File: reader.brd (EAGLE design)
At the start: 41.6 x 39.4 mm, 15 parts, among them J1 RJ11-6PTH, J2 AVR_SPI_PRG_6NS

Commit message: Change sound source select jumpers to a single 3-pin jumper
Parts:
- removed JP3: (no value), SparkFun-Retired:1X02
- JP2: device SparkFun-Retired:1X02 -> jumper:JP2
- moved JP2 1.27 mm to (20.3, 25.4), turned to 90 degrees
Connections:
- removed net N$4: JP2.2, JP3.2, SP1.1
- new net N$1: JP2.2, SP1.1
- net N$9: now also JP2.3; no longer JP3.1
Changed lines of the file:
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@@
 <element name="J2" library="SparkFun-Connectors" package="2X3-NS" value="AVR_SPI_PRG_6NS" x="35.56" y="34.29"/>
 <element name="JP1" library="SparkFun-Connectors" package="1X08" value="MFRC522 Module" x="25.4" y="10.16" rot="R90"/>
-<element name="JP2" library="SparkFun-Retired" package="1X02" value="" x="19.05" y="25.4" rot="R270"/>
-<element name="JP3" library="SparkFun-Retired" package="1X02" value="" x="21.59" y="25.4" rot="R270"/>
 <element name="LD1" library="led" package="DUOLED-C-5MM" value="STATUS" x="1.27" y="34.29" rot="R90"/>
 <element name="LED1" library="led" package="LED3MM" value="BLUE" x="1.27" y="2.54" rot="R90"/>
@@
 <attribute name="OC_FARNELL" value="unknown" x="11.43" y="11.43" size="1.778" layer="27" rot="R180" display="off"/>
 </element>
+<element name="JP2" library="jumper" package="JP2" value="" x="20.32" y="25.4" rot="R90"/>
 </elements>
 <signals>
@@
 </signal>
 <signal name="EXT_SPEAKER">
+<contactref element="J1" pad="6"/>
 <contactref element="JP2" pad="1"/>
-<contactref element="J1" pad="6"/>
-<wire x1="6.985" y1="27.94" x2="19.05" y2="25.4" width="0" layer="19" extent="1-1"/>
+<wire x1="20.32" y1="22.86" x2="6.985" y2="27.94" width="0" layer="19" extent="1-1"/>
 </signal>
 <signal name="SPEAKER">
@@
 </signal>
 <signal name="N$9">
-<contactref element="JP3" pad="1"/>
 <contactref element="R4" pad="2"/>
-<wire x1="21.59" y1="25.4" x2="38.1" y2="27.57" width="0" layer="19" extent="16-16"/>
+<contactref element="JP2" pad="3"/>
+<wire x1="20.32" y1="27.94" x2="38.1" y2="27.57" width="0" layer="19" extent="16-16"/>
 </signal>
-<signal name="N$4">
+<signal name="N$1">
+<contactref element="SP1" pad="1"/>
 <contactref element="JP2" pad="2"/>
-<contactref element="JP3" pad="2"/>
-<contactref element="SP1" pad="1"/>
-<wire x1="19.05" y1="22.86" x2="21.59" y2="22.86" width="0" layer="19" extent="1-1"/>
-<wire x1="16.4338" y1="11.43" x2="19.05" y2="22.86" width="0" layer="19" extent="1-1"/>
+<wire x1="20.32" y1="25.4" x2="16.4338" y2="11.43" width="0" layer="19" extent="1-1"/>
 </signal>
 </signals>

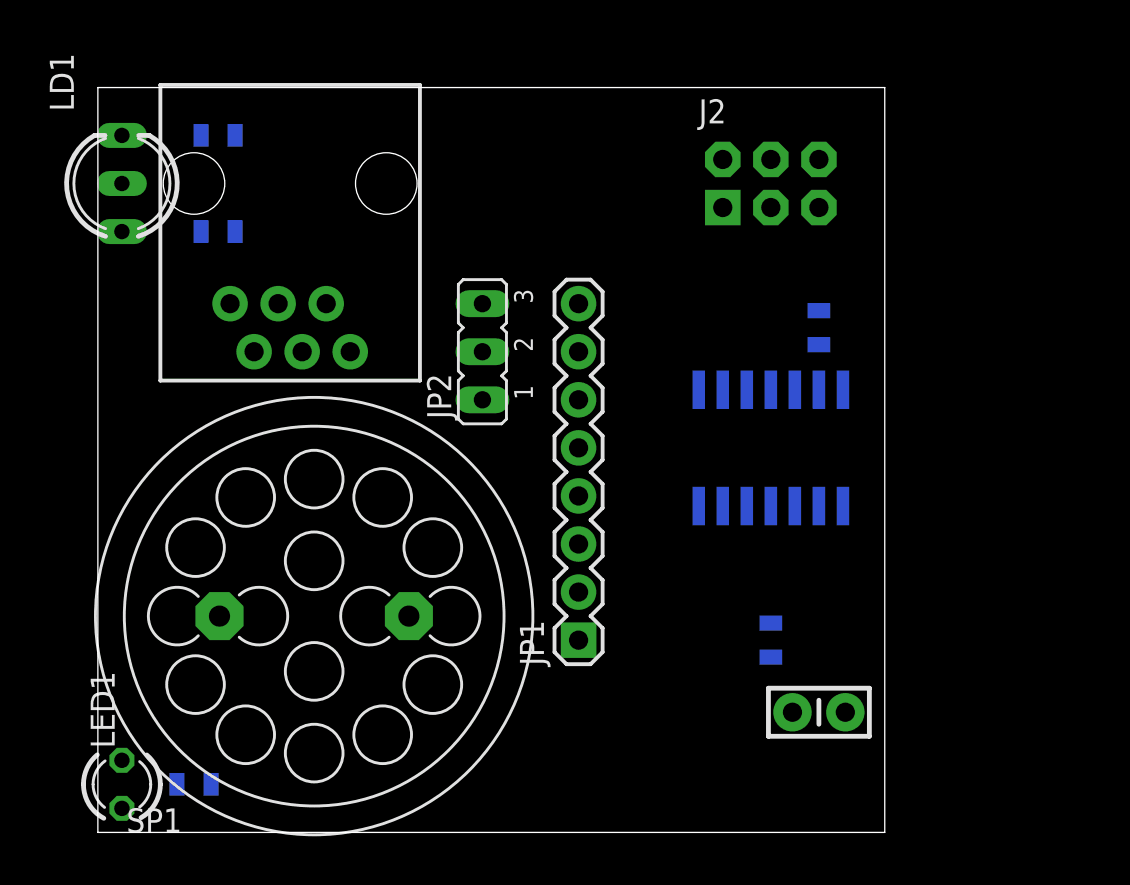
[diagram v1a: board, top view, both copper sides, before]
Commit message: Route reader board prototype
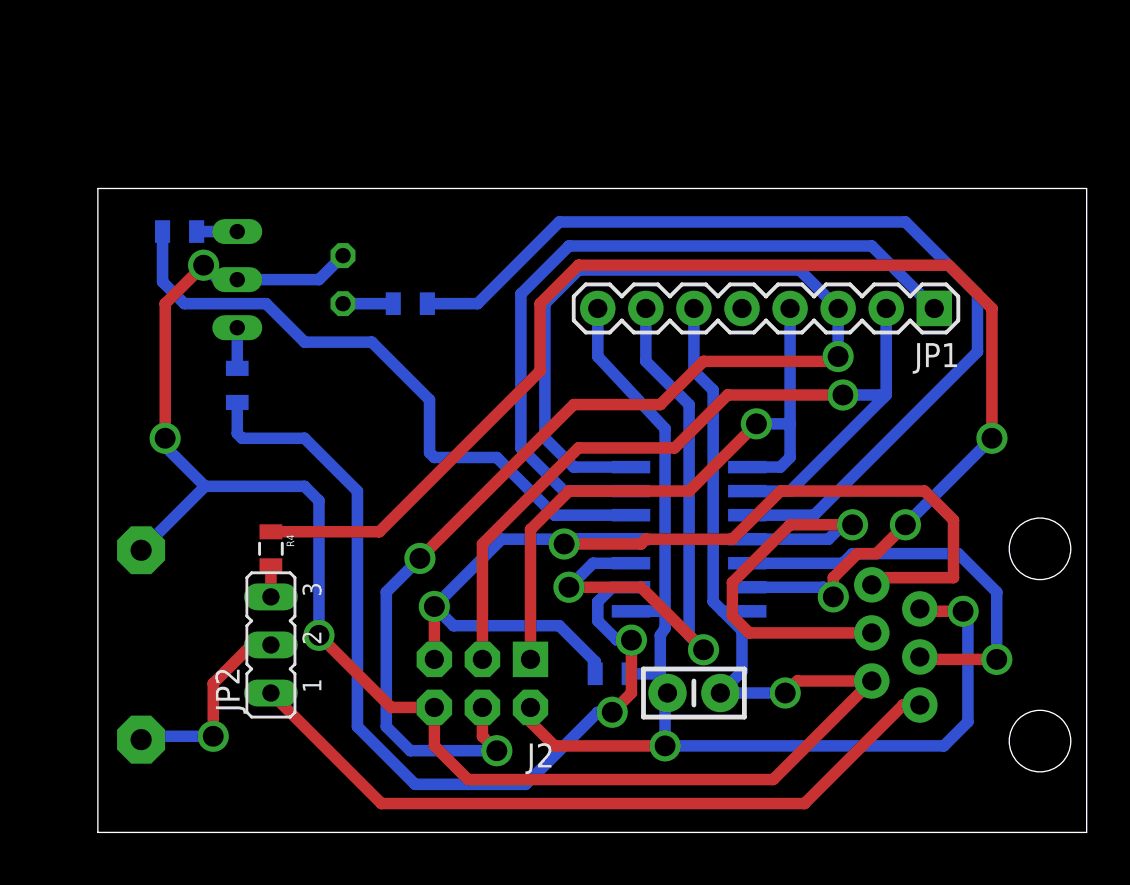
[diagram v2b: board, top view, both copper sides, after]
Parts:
- moved J1 39.6 mm to (49.8, 15.0), flipped to the bottom, turned to 270 degrees
- moved R4 31.2 mm to (9.14, 15.0), flipped to the top, turned to 270 degrees
- moved J2 30.5 mm to (20.3, 7.87), turned to 180 degrees
- moved LED1 29.1 mm to (13.0, 29.2), flipped to the bottom
- moved R3 27.9 mm to (16.5, 27.9)
- moved JP1 25.7 mm to (44.2, 27.7), turned to 180 degrees
- moved JP2 19.1 mm to (9.14, 9.91)
- moved R1 13.2 mm to (7.37, 23.6), turned to 270 degrees
- moved SP1 9.27 mm to (2.29, 9.91), flipped to the bottom, turned to 90 degrees
- moved R5 8.57 mm to (27.2, 8.38), turned to 0 degrees
- moved LD1 7.94 mm to (7.37, 29.2), flipped to the bottom, turned to 270 degrees
- moved C1 6.68 mm to (31.5, 7.37)
- moved U$1 6.48 mm to (31.2, 15.5), turned to 90 degrees
- moved R2 2.03 mm to (4.32, 31.8), turned to 0 degrees
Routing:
- net GND: track 0.00 -> 106.9 mm, vias 0 -> 4
- net MOSI: track 0.00 -> 77.0 mm, vias 0 -> 3
- net SPEAKER: track 0.00 -> 71.0 mm, vias 0 -> 3
- net VCC: track 0.00 -> 61.4 mm, vias 0 -> 2
- net RST: track 0.00 -> 58.8 mm, vias 0 -> 2
- net BLUE_LED: track 0.00 -> 51.2 mm
- net RED_LED: track 0.00 -> 47.5 mm, vias 0 -> 2
- net SCK: track 0.00 -> 44.6 mm, vias 0 -> 1
- net RDR_SS: track 0.00 -> 39.2 mm
- net EXT_SPEAKER: track 0.00 -> 38.9 mm
- net GREEN_LED: track 0.00 -> 34.2 mm
- net MISO: track 0.00 -> 33.2 mm, vias 0 -> 1
- net RDR_RESET: track 0.00 -> 31.6 mm, vias 0 -> 2
- net CONTROLLER_RXD: track 0.00 -> 23.0 mm, vias 0 -> 1
- net CONTROLLER_TXD: track 0.00 -> 21.9 mm, vias 0 -> 1
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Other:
- board size 41.6 x 39.4 mm -> 52.2 x 34 mm

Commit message: Move the reader connector to the top of the board, reroute accordingly
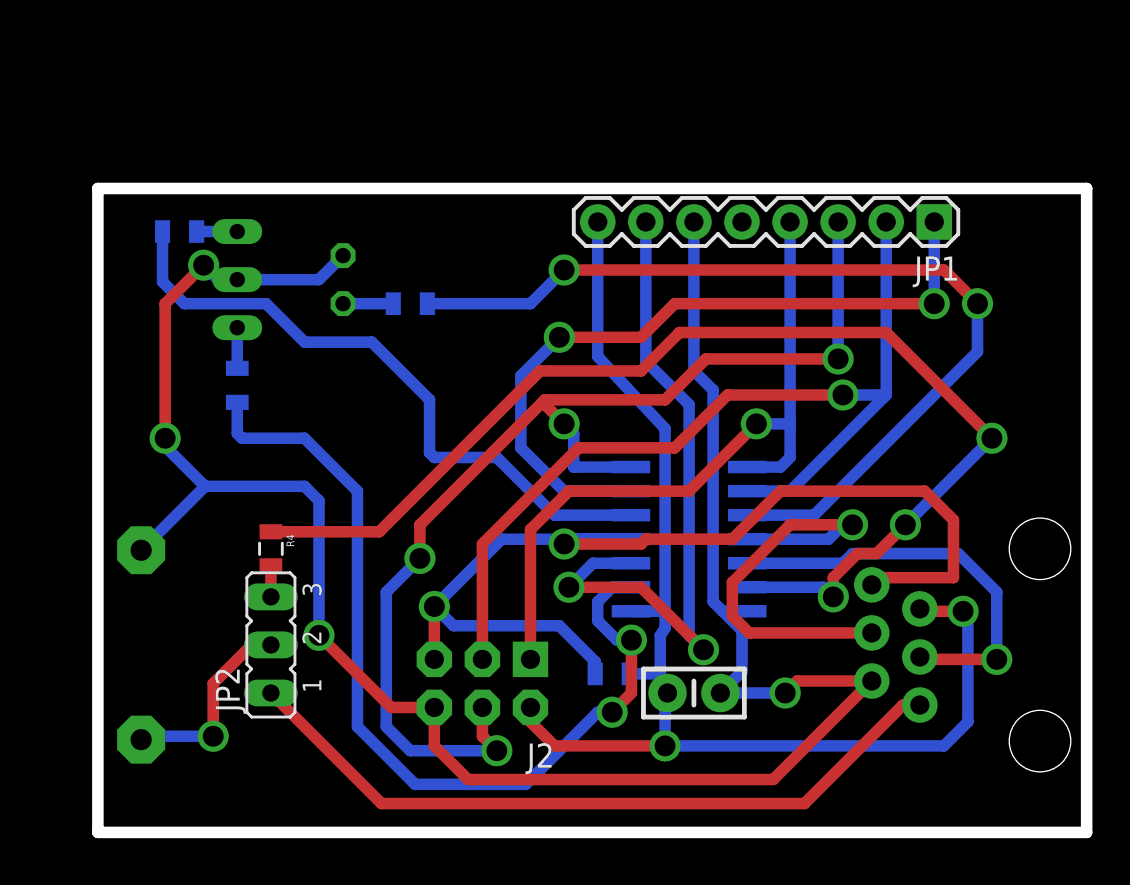
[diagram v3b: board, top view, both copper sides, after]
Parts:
- moved JP1 4.57 mm to (44.2, 32.3)
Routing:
- net MOSI: track 77.0 -> 60.5 mm, vias 3 -> 4
- net SPEAKER: track 71.0 -> 62.0 mm
- net SCK: track 44.6 -> 49.2 mm
- net RDR_RESET: track 31.6 -> 36.2 mm
- net MISO: track 33.2 -> 37.8 mm
- net GND: track 106.9 -> 111.5 mm
- net VCC: track 61.4 -> 65.9 mm
- net BLUE_LED: track 51.2 -> 48.8 mm, vias 0 -> 2
- net RDR_SS: track 39.2 -> 38.3 mm, vias 0 -> 2
